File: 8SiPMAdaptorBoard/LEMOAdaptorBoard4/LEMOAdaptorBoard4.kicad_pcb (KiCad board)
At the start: 2 copper layers, 51.1 x 69.5 mm, 21 parts

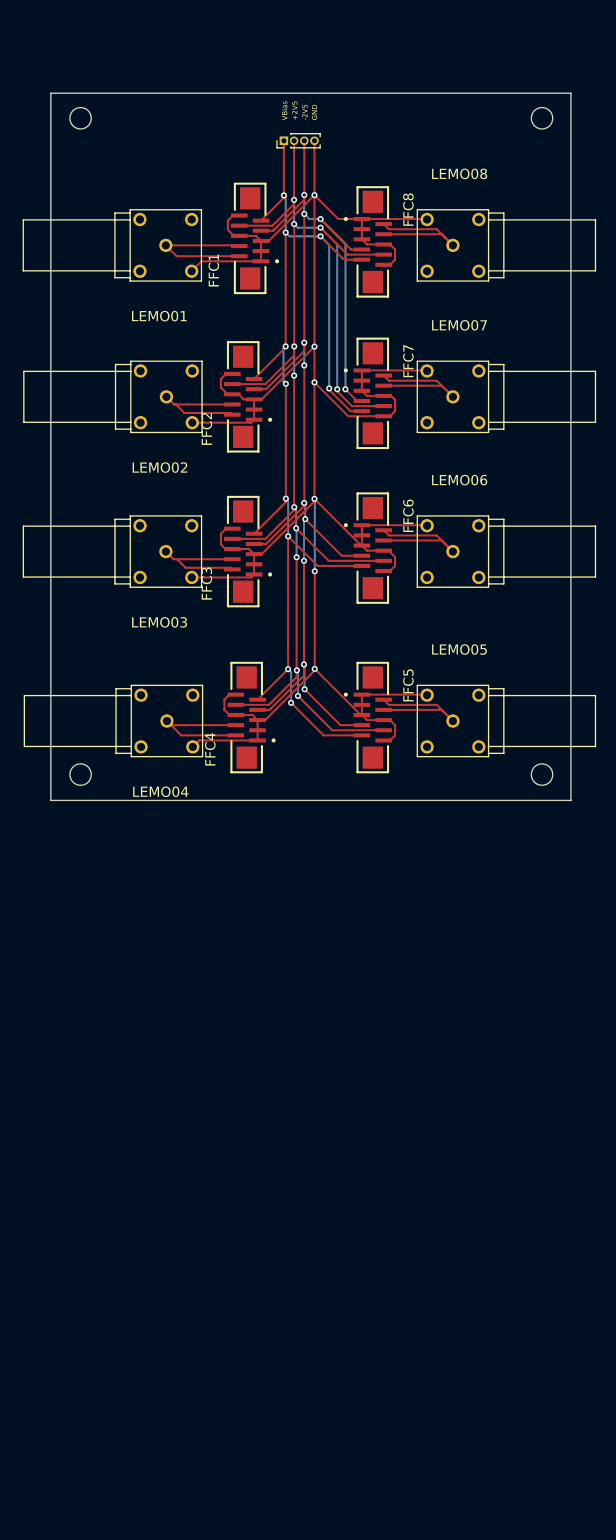
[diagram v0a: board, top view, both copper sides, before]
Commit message: Update LEMOAdaptorBoard4 for horizontal FFC connector
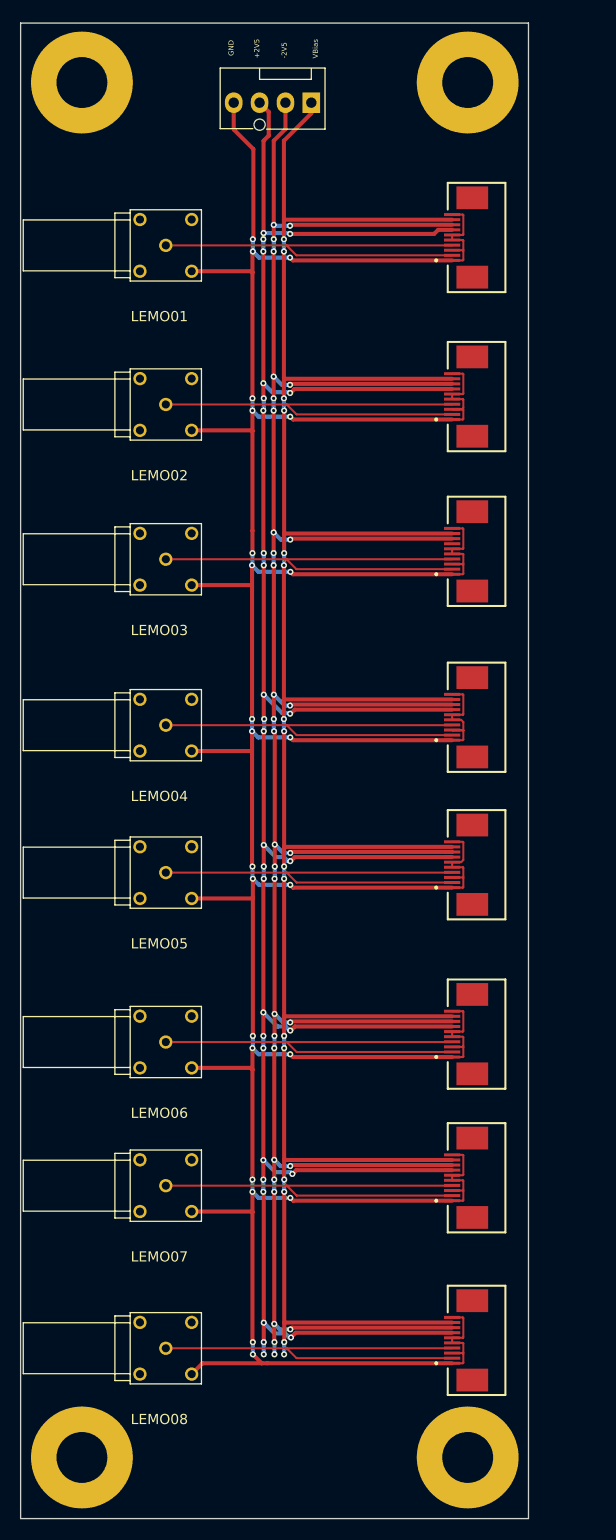
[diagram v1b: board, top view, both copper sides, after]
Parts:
- removed REF** (x4): MountingHole_2.1mm, MountingHole:MountingHole_2.1mm
- added H1: MountingHole_Pad, MountingHole:MountingHole_5mm_Pad, F.Cu at (46.2, 55.3)
- added H2: MountingHole_Pad, MountingHole:MountingHole_5mm_Pad, F.Cu at (84.0, 55.3)
- added H3: MountingHole_Pad, MountingHole:MountingHole_5mm_Pad, F.Cu at (46.2, 190.3)
- added H4: MountingHole_Pad, MountingHole:MountingHole_5mm_Pad, F.Cu at (84.0, 190.3)
- FFC1, FFC2, FFC3, FFC4, FFC5, FFC6, FFC7, FFC8: footprint FFC_10position_vertical:SAMTEC_ZF5S-10-03-T-WT -> FFC_10position_connector:SAMTEC_ZF5S-10-01-T-WT
- Power1: footprint Connector_PinHeader_1.00mm:PinHeader_1x04_P1.00mm_Vertical -> Connector:FanPinHeader_1x04_P2.54mm_Vertical
- moved LEMO08 111.9 mm to (54.4, 179.6), turned to 180 degrees
- moved FFC8 108.3 mm to (84.5, 178.8), turned to 90 degrees
- moved LEMO07 82.4 mm to (54.4, 163.6), turned to 180 degrees
- moved FFC7 77.7 mm to (84.5, 162.8), turned to 90 degrees
- moved LEMO06 55.8 mm to (54.4, 149.5), turned to 180 degrees
- moved FFC6 48.7 mm to (84.5, 148.7), turned to 90 degrees
- moved LEMO05 31.9 mm to (54.4, 132.9), turned to 180 degrees
- moved FFC2 22.5 mm to (84.5, 86.1)
- moved FFC3 22.5 mm to (84.5, 101.3)
- moved FFC4 22.2 mm to (84.5, 117.6)
- moved FFC1 21.8 mm to (84.5, 70.5)
- moved FFC5 17.4 mm to (84.5, 132.1), turned to 90 degrees
- moved Power1 4.61 mm to (68.7, 57.3), turned to 180 degrees
- moved LEMO02 0.75 mm to (54.4, 86.9)
- moved LEMO03 0.75 mm to (54.4, 102.1)
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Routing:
- net Net-(Power1-Pin_4): track 226.8 -> 415.7 mm, vias 6 -> 23
- net Net-(FFC1-V_Bias): track 117.4 -> 256.2 mm, vias 10 -> 16
- net Net-(FFC1--2V5): track 122.1 -> 258.2 mm, vias 11 -> 30
- net Net-(FFC1-+2V5): track 136.5 -> 266.0 mm, vias 11 -> 32
- net Net-(FFC3-Signal-Pad02): track 12.7 -> 45.0 mm
- net Net-(FFC2-Signal-Pad02): track 12.7 -> 45.1 mm
- net Net-(FFC4-Signal-Pad02): track 14.3 -> 44.9 mm
- net Net-(FFC6-Signal-Pad02): track 14.9 -> 45.1 mm
- net Net-(FFC5-Signal-Pad02): track 14.9 -> 45.0 mm
- net Net-(FFC7-Signal-Pad02): track 14.9 -> 44.9 mm
- net Net-(FFC8-Signal-Pad02): track 14.9 -> 44.9 mm
- net Net-(FFC1-Signal-Pad02): track 14.9 -> 44.8 mm
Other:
- board size 51.1 x 69.5 mm -> 49.9 x 146.9 mm
- board text removed: "UST Phys SiPM adaptor board 2024 03 26 Eltis"

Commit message: More update
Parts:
- added Power2: Conn_01x04, Connector:FanPinHeader_1x04_P2.54mm_Vertical, F.Cu at (68.2, 188.1)
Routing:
- net Net-(Power1-Pin_4): track 415.7 -> 425.2 mm
- net Net-(FFC1-V_Bias): track 256.2 -> 265.0 mm, vias 16 -> 17
- net Net-(FFC1--2V5): track 258.2 -> 266.5 mm, vias 30 -> 31
- net Net-(FFC1-+2V5): track 266.0 -> 274.1 mm, vias 32 -> 33
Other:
- board size 49.9 x 146.9 mm -> 49.9 x 147.2 mm

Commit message: More update
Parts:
- Power1, Power2: footprint Connector:FanPinHeader_1x04_P2.54mm_Vertical -> Connector_PinHeader_2.54mm:PinHeader_1x04_P2.54mm_Horizontal
- moved Power1 8.13 mm to (61.5, 61.1), turned to 90 degrees
- moved Power2 2.31 mm to (68.0, 185.8), turned to -90 degrees
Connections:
- net Net-(FFC1-+2V5) renamed /+2V5
- net Net-(FFC1--2V5) renamed /-2V5
- net Net-(FFC1-V_Bias) renamed /V_Bias
- FFC1 pad 01: Net-(Power1-Pin_4) -> /Earth
- FFC1 pad 02: Net-(FFC1-Signal-Pad02) -> /Signal
- FFC1 pad 03: Net-(Power1-Pin_4) -> /Earth
- FFC1 pad 04: Net-(FFC1-Signal-Pad02) -> /Signal
- FFC1 pad 05: Net-(Power1-Pin_4) -> /Earth
- FFC1 pad 06: Net-(Power1-Pin_4) -> /Earth
- FFC1 pad 10: Net-(Power1-Pin_4) -> /Earth
- FFC1 pad S1: (no net) -> /Earth
- FFC1 pad S2: (no net) -> /Earth
- FFC2 pad 01: Net-(Power1-Pin_4) -> /Earth
- FFC2 pad 02: Net-(FFC2-Signal-Pad02) -> /Signal
- FFC2 pad 03: Net-(Power1-Pin_4) -> /Earth
- FFC2 pad 04: Net-(FFC2-Signal-Pad02) -> /Signal
- FFC2 pad 05: Net-(Power1-Pin_4) -> /Earth
- FFC2 pad 06: Net-(Power1-Pin_4) -> /Earth
- FFC2 pad 10: Net-(Power1-Pin_4) -> /Earth
- FFC2 pad S1: (no net) -> /Earth
- FFC2 pad S2: (no net) -> /Earth
- FFC3 pad 01: Net-(Power1-Pin_4) -> /Earth
- FFC3 pad 02: Net-(FFC3-Signal-Pad02) -> /Signal
- FFC3 pad 03: Net-(Power1-Pin_4) -> /Earth
- FFC3 pad 04: Net-(FFC3-Signal-Pad02) -> /Signal
- FFC3 pad 05: Net-(Power1-Pin_4) -> /Earth
- FFC3 pad 06: Net-(Power1-Pin_4) -> /Earth
- FFC3 pad 10: Net-(Power1-Pin_4) -> /Earth
- FFC3 pad S1: (no net) -> /Earth
- FFC3 pad S2: (no net) -> /Earth
- FFC4 pad 01: Net-(Power1-Pin_4) -> /Earth
- FFC4 pad 02: Net-(FFC4-Signal-Pad02) -> /Signal
- FFC4 pad 03: Net-(Power1-Pin_4) -> /Earth
- FFC4 pad 04: Net-(FFC4-Signal-Pad02) -> /Signal
- FFC4 pad 05: Net-(Power1-Pin_4) -> /Earth
- FFC4 pad 06: Net-(Power1-Pin_4) -> /Earth
- FFC4 pad 10: Net-(Power1-Pin_4) -> /Earth
- FFC4 pad S1: (no net) -> /Earth
- FFC4 pad S2: (no net) -> /Earth
- FFC5 pad 01: Net-(Power1-Pin_4) -> /Earth
- FFC5 pad 02: Net-(FFC5-Signal-Pad02) -> /Signal
- FFC5 pad 03: Net-(Power1-Pin_4) -> /Earth
- FFC5 pad 04: Net-(FFC5-Signal-Pad02) -> /Signal
- FFC5 pad 05: Net-(Power1-Pin_4) -> /Earth
- FFC5 pad 06: Net-(Power1-Pin_4) -> /Earth
- FFC5 pad 10: Net-(Power1-Pin_4) -> /Earth
- FFC5 pad S1: (no net) -> /Earth
- FFC5 pad S2: (no net) -> /Earth
- FFC6 pad 01: Net-(Power1-Pin_4) -> /Earth
- FFC6 pad 02: Net-(FFC6-Signal-Pad02) -> /Signal
- FFC6 pad 03: Net-(Power1-Pin_4) -> /Earth
- FFC6 pad 04: Net-(FFC6-Signal-Pad02) -> /Signal
- FFC6 pad 05: Net-(Power1-Pin_4) -> /Earth
- FFC6 pad 06: Net-(Power1-Pin_4) -> /Earth
- FFC6 pad 10: Net-(Power1-Pin_4) -> /Earth
- FFC6 pad S1: (no net) -> /Earth
- FFC6 pad S2: (no net) -> /Earth
- FFC7 pad 01: Net-(Power1-Pin_4) -> /Earth
- FFC7 pad 02: Net-(FFC7-Signal-Pad02) -> /Signal
- FFC7 pad 03: Net-(Power1-Pin_4) -> /Earth
- FFC7 pad 04: Net-(FFC7-Signal-Pad02) -> /Signal
- FFC7 pad 05: Net-(Power1-Pin_4) -> /Earth
- FFC7 pad 06: Net-(Power1-Pin_4) -> /Earth
- FFC7 pad 10: Net-(Power1-Pin_4) -> /Earth
- FFC7 pad S1: (no net) -> /Earth
- FFC7 pad S2: (no net) -> /Earth
- FFC8 pad 01: Net-(Power1-Pin_4) -> /Earth
- FFC8 pad 02: Net-(FFC8-Signal-Pad02) -> /Signal
- FFC8 pad 03: Net-(Power1-Pin_4) -> /Earth
- FFC8 pad 04: Net-(FFC8-Signal-Pad02) -> /Signal
- FFC8 pad 05: Net-(Power1-Pin_4) -> /Earth
- FFC8 pad 06: Net-(Power1-Pin_4) -> /Earth
- FFC8 pad 10: Net-(Power1-Pin_4) -> /Earth
- FFC8 pad S1: (no net) -> /Earth
- FFC8 pad S2: (no net) -> /Earth
- LEMO01 pad 1: Net-(FFC1-Signal-Pad02) -> /Signal
- LEMO01 pad SHIELD1: Net-(Power1-Pin_4) -> /Earth
- LEMO01 pad SHIELD2: unconnected-(LEMO01-PadSHIELD2) -> /Earth
- LEMO01 pad SHIELD3: unconnected-(LEMO01-PadSHIELD3) -> /Earth
- LEMO01 pad SHIELD4: unconnected-(LEMO01-PadSHIELD4) -> /Earth
- LEMO02 pad 1: Net-(FFC2-Signal-Pad02) -> /Signal
- LEMO02 pad SHIELD1: Net-(Power1-Pin_4) -> /Earth
- LEMO02 pad SHIELD2: unconnected-(LEMO02-PadSHIELD2) -> /Earth
- LEMO02 pad SHIELD3: unconnected-(LEMO02-PadSHIELD3) -> /Earth
- LEMO02 pad SHIELD4: unconnected-(LEMO02-PadSHIELD4) -> /Earth
- LEMO03 pad 1: Net-(FFC3-Signal-Pad02) -> /Signal
- LEMO03 pad SHIELD1: Net-(Power1-Pin_4) -> /Earth
- LEMO03 pad SHIELD2: unconnected-(LEMO03-PadSHIELD2) -> /Earth
- LEMO03 pad SHIELD3: unconnected-(LEMO03-PadSHIELD3) -> /Earth
- LEMO03 pad SHIELD4: unconnected-(LEMO03-PadSHIELD4) -> /Earth
- LEMO04 pad 1: Net-(FFC4-Signal-Pad02) -> /Signal
- LEMO04 pad SHIELD1: Net-(Power1-Pin_4) -> /Earth
- LEMO04 pad SHIELD2: unconnected-(LEMO04-PadSHIELD2) -> /Earth
- LEMO04 pad SHIELD3: unconnected-(LEMO04-PadSHIELD3) -> /Earth
- LEMO04 pad SHIELD4: unconnected-(LEMO04-PadSHIELD4) -> /Earth
- LEMO05 pad 1: Net-(FFC5-Signal-Pad02) -> /Signal
- LEMO05 pad SHIELD1: Net-(Power1-Pin_4) -> /Earth
- LEMO05 pad SHIELD2: unconnected-(LEMO05-PadSHIELD2) -> /Earth
- LEMO05 pad SHIELD3: unconnected-(LEMO05-PadSHIELD3) -> /Earth
- LEMO05 pad SHIELD4: unconnected-(LEMO05-PadSHIELD4) -> /Earth
- LEMO06 pad 1: Net-(FFC6-Signal-Pad02) -> /Signal
- LEMO06 pad SHIELD1: Net-(Power1-Pin_4) -> /Earth
- LEMO06 pad SHIELD2: unconnected-(LEMO06-PadSHIELD2) -> /Earth
- LEMO06 pad SHIELD3: unconnected-(LEMO06-PadSHIELD3) -> /Earth
- LEMO06 pad SHIELD4: unconnected-(LEMO06-PadSHIELD4) -> /Earth
- LEMO07 pad 1: Net-(FFC7-Signal-Pad02) -> /Signal
- LEMO07 pad SHIELD1: Net-(Power1-Pin_4) -> /Earth
- LEMO07 pad SHIELD2: unconnected-(LEMO07-PadSHIELD2) -> /Earth
- LEMO07 pad SHIELD3: unconnected-(LEMO07-PadSHIELD3) -> /Earth
- LEMO07 pad SHIELD4: unconnected-(LEMO07-PadSHIELD4) -> /Earth
- LEMO08 pad 1: Net-(FFC8-Signal-Pad02) -> /Signal
- LEMO08 pad SHIELD1: Net-(Power1-Pin_4) -> /Earth
- LEMO08 pad SHIELD2: unconnected-(LEMO08-PadSHIELD2) -> /Earth
- LEMO08 pad SHIELD3: unconnected-(LEMO08-PadSHIELD3) -> /Earth
- LEMO08 pad SHIELD4: unconnected-(LEMO08-PadSHIELD4) -> /Earth
- Power1 pad 4: Net-(Power1-Pin_4) -> /Earth
- Power2 pad 4: Net-(Power1-Pin_4) -> /Earth
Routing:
- net Net-(Power1-Pin_4): track 425.2 -> 0.00 mm, vias 23 -> 0
- net /Signal: track 0.00 -> 359.7 mm
- net Net-(FFC6-Signal-Pad02): track 45.1 -> 0.00 mm
- net Net-(FFC2-Signal-Pad02): track 45.1 -> 0.00 mm
- net Net-(FFC3-Signal-Pad02): track 45.0 -> 0.00 mm
- net Net-(FFC5-Signal-Pad02): track 45.0 -> 0.00 mm
- net Net-(FFC4-Signal-Pad02): track 44.9 -> 0.00 mm
- net Net-(FFC7-Signal-Pad02): track 44.9 -> 0.00 mm
- net Net-(FFC8-Signal-Pad02): track 44.9 -> 0.00 mm
- net Net-(FFC1-Signal-Pad02): track 44.8 -> 0.00 mm
- net /+2V5: track 274.1 -> 268.5 mm, vias 33 -> 34
- net /-2V5: track 266.5 -> 261.1 mm
- net /V_Bias: track 265.0 -> 259.9 mm
- added copper zone on B.Cu, net /Earth
- added copper zone on F.Cu, net /Earth

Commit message: More update
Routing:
- net /Earth: track 0.00 -> 88.4 mm
- net /-2V5: track 261.1 -> 280.5 mm, vias 31 -> 32
- net /V_Bias: vias 17 -> 16
- net /+2V5: vias 34 -> 33

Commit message: More update
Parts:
- Power1: moved to B.Cu
- moved Power1 7.25 mm to (68.8, 60.8)
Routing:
- net /+2V5: track 268.5 -> 268.9 mm, vias 33 -> 32

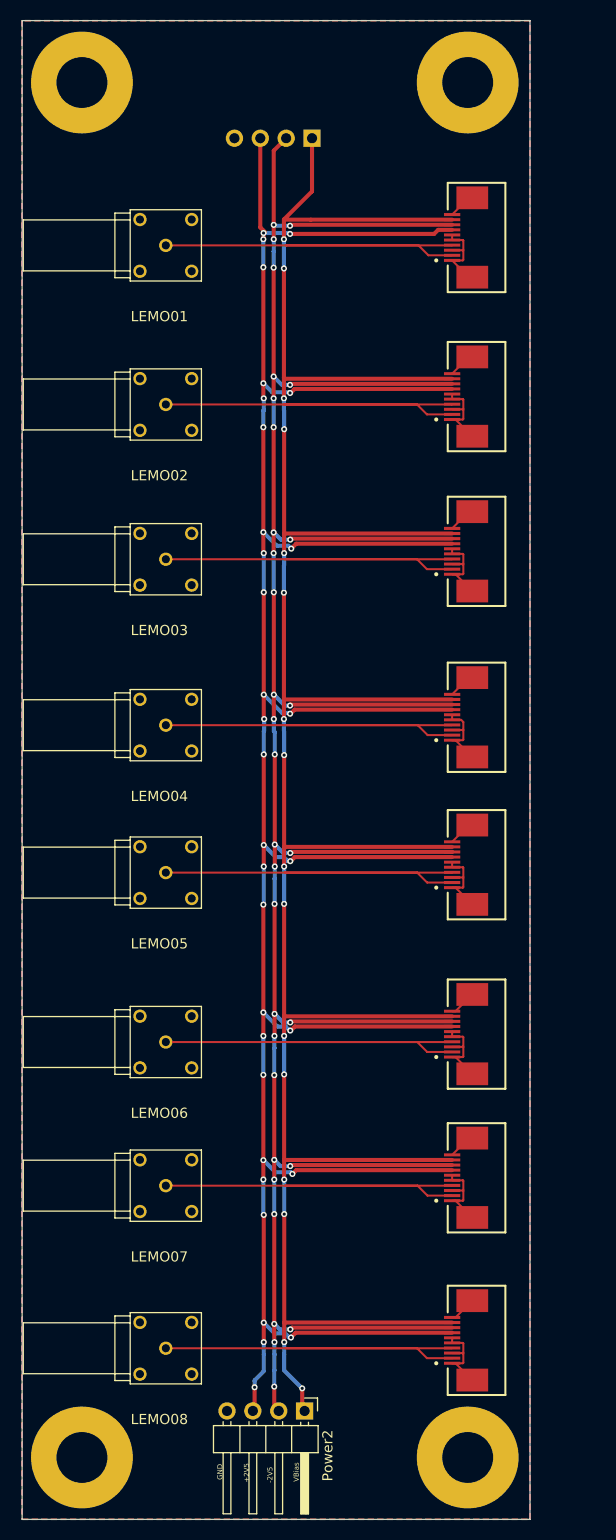
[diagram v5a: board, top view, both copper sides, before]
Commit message: re-rount traces to pass JLC DFM
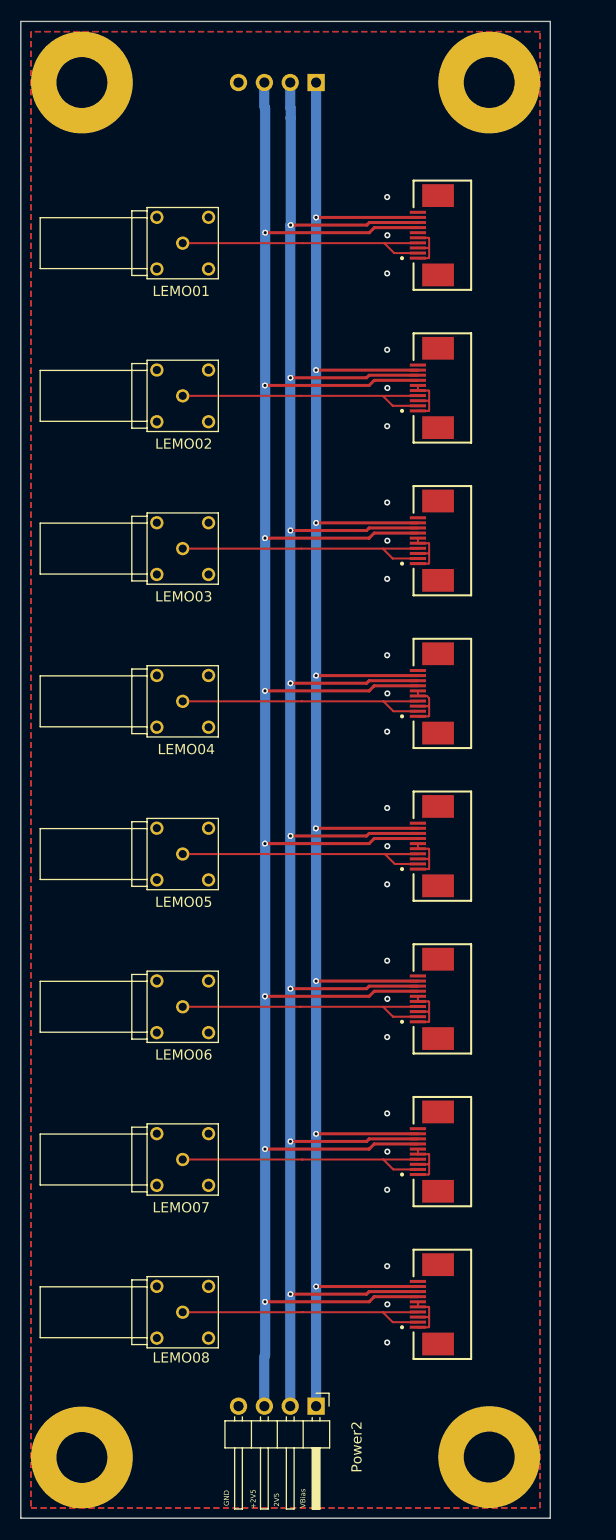
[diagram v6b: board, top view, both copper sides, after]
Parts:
- moved Power1 5.48 mm to (69.2, 55.3)
- moved FFC8 4.88 mm to (81.1, 175.3)
- moved FFC6 4.82 mm to (81.1, 145.3)
- moved FFC7 4.23 mm to (81.1, 160.3)
- moved FFC4 4.10 mm to (81.1, 115.3)
- moved LEMO08 3.91 mm to (56.1, 176.1)
- moved LEMO06 3.84 mm to (56.1, 146.1)
- moved FFC5 3.82 mm to (81.1, 130.3)
- moved FFC3 3.52 mm to (81.1, 100.3)
- moved FFC2 3.46 mm to (81.1, 85.3)
- moved FFC1 3.37 mm to (81.1, 70.3)
- moved LEMO07 3.06 mm to (56.1, 161.1)
- moved LEMO04 2.87 mm to (56.1, 116.1)
- moved LEMO05 2.47 mm to (56.1, 131.1)
- moved H4 2.11 mm to (86.2, 190.3)
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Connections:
- FFC1 pad 02: /Signal -> /Signal1
- FFC1 pad 04: /Signal -> /Signal1
- FFC2 pad 02: /Signal -> /Signal2
- FFC2 pad 04: /Signal -> /Signal2
- FFC3 pad 02: /Signal -> /Signal3
- FFC3 pad 04: /Signal -> /Signal3
- FFC4 pad 02: /Signal -> /Signal4
- FFC4 pad 04: /Signal -> /Signal4
- FFC5 pad 02: /Signal -> /Signal5
- FFC5 pad 04: /Signal -> /Signal5
- FFC6 pad 02: /Signal -> /Signal6
- FFC6 pad 04: /Signal -> /Signal6
- FFC7 pad 02: /Signal -> /Signal7
- FFC7 pad 04: /Signal -> /Signal7
- FFC8 pad 02: /Signal -> /Signal8
- FFC8 pad 04: /Signal -> /Signal8
- LEMO01 pad 1: /Signal -> /Signal1
- LEMO02 pad 1: /Signal -> /Signal2
- LEMO03 pad 1: /Signal -> /Signal3
- LEMO04 pad 1: /Signal -> /Signal4
- LEMO05 pad 1: /Signal -> /Signal5
- LEMO06 pad 1: /Signal -> /Signal6
- LEMO07 pad 1: /Signal -> /Signal7
- LEMO08 pad 1: /Signal -> /Signal8
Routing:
- net /Signal: track 359.7 -> 0.00 mm
- net /V_Bias: track 259.5 -> 212.1 mm, vias 16 -> 8
- net /Earth: track 88.4 -> 50.0 mm, vias 0 -> 24
- net /+2V5: track 268.9 -> 230.9 mm, vias 32 -> 8
- net /Signal5: track 0.00 -> 30.0 mm
- net /-2V5: track 280.1 -> 251.7 mm, vias 32 -> 8
- net /Signal3: track 0.00 -> 27.0 mm
- net /Signal2: track 0.00 -> 27.0 mm
- net /Signal8: track 0.00 -> 27.0 mm
- net /Signal6: track 0.00 -> 26.9 mm
- net /Signal7: track 0.00 -> 26.9 mm
- net /Signal4: track 0.00 -> 26.9 mm
- net /Signal1: track 0.00 -> 26.8 mm
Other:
- board size 49.9 x 147.2 mm -> 52 x 147 mm

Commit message: move power inward, add text description
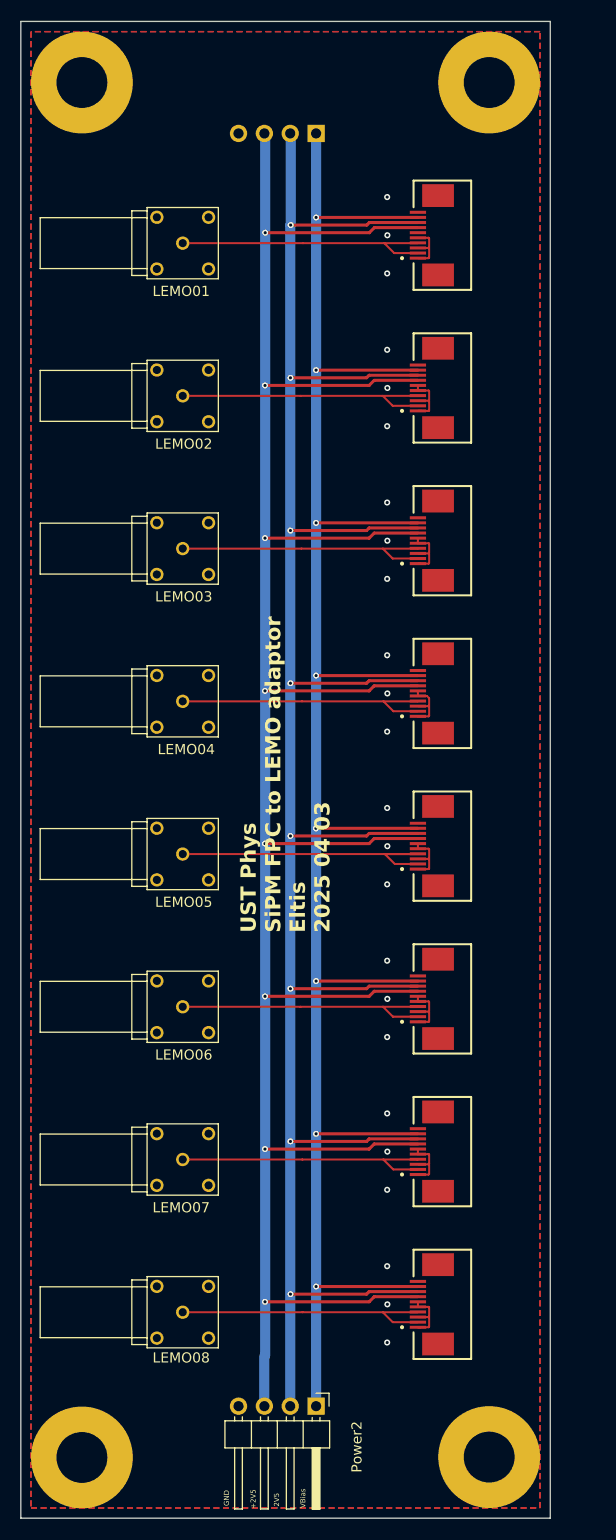
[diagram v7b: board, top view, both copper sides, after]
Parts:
- moved Power1 5.00 mm to (69.2, 60.3)
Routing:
- net /V_Bias: track 212.1 -> 207.1 mm
- net /-2V5: track 251.7 -> 246.7 mm
- net /+2V5: track 230.9 -> 225.9 mm
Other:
- board text added: "UST Phys SiPM FPC to LEMO adaptor Eltis 2025 04 03"
